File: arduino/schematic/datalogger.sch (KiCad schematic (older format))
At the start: 14 parts

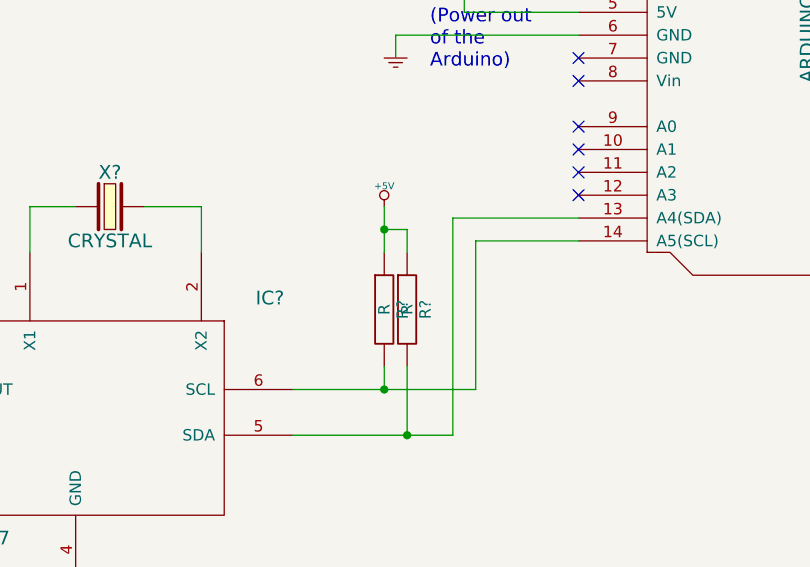
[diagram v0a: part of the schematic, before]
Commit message: Added last values to schematic and made PDF for quick viewing
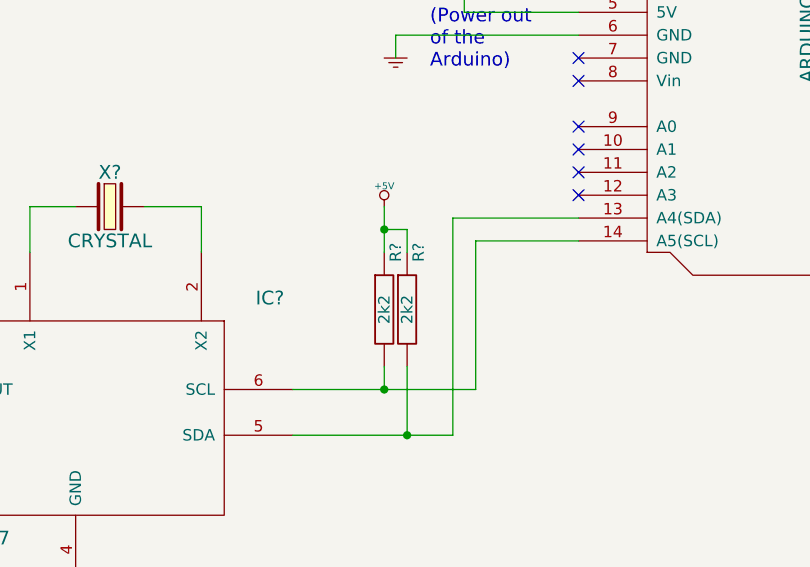
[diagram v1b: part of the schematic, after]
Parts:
- R? (x2): value R -> 2k2
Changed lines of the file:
@@
-EESchema Schematic File Version 2  date Thu 24 May 2012 22:24:53 BST
+EESchema Schematic File Version 2  date Fri 25 May 2012 22:57:14 BST
 LIBS:74xx
 LIBS:adc-dac
@@
 LIBS:valves
 LIBS:xilinx
-EELAYER 43  0
+EELAYER 25  0
 EELAYER END
 $Descr A4 11700 8267
 encoding utf-8
 Sheet 1 1
-Title ""
-Date "24 may 2012"
+Title "Arduino temperature datalogger"
+Date "25 may 2012"
 Rev ""
-Comp ""
+Comp "nathandumont.com"
 Comment1 ""
 Comment2 ""
@@
 U 1 1 4FBE9F9A
 P 5350 5200
-F 0 "R?" V 5430 5200 50  0000 C CNN
-F 1 "R" V 5350 5200 50  0000 C CNN
+F 0 "R?" V 5400 5450 50  0000 C CNN
+F 1 "2k2" V 5350 5200 50  0000 C CNN
 	1    5350 5200
 	1    0    0    -1
@@
 U 1 1 4FBE9F96
 P 5450 5200
-F 0 "R?" V 5530 5200 50  0000 C CNN
-F 1 "R" V 5450 5200 50  0000 C CNN
+F 0 "R?" V 5500 5450 50  0000 C CNN
+F 1 "2k2" V 5450 5200 50  0000 C CNN
 	1    5450 5200
 	1    0    0    -1
